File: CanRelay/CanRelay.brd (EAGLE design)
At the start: 84.6 x 65.5 mm, 20 parts

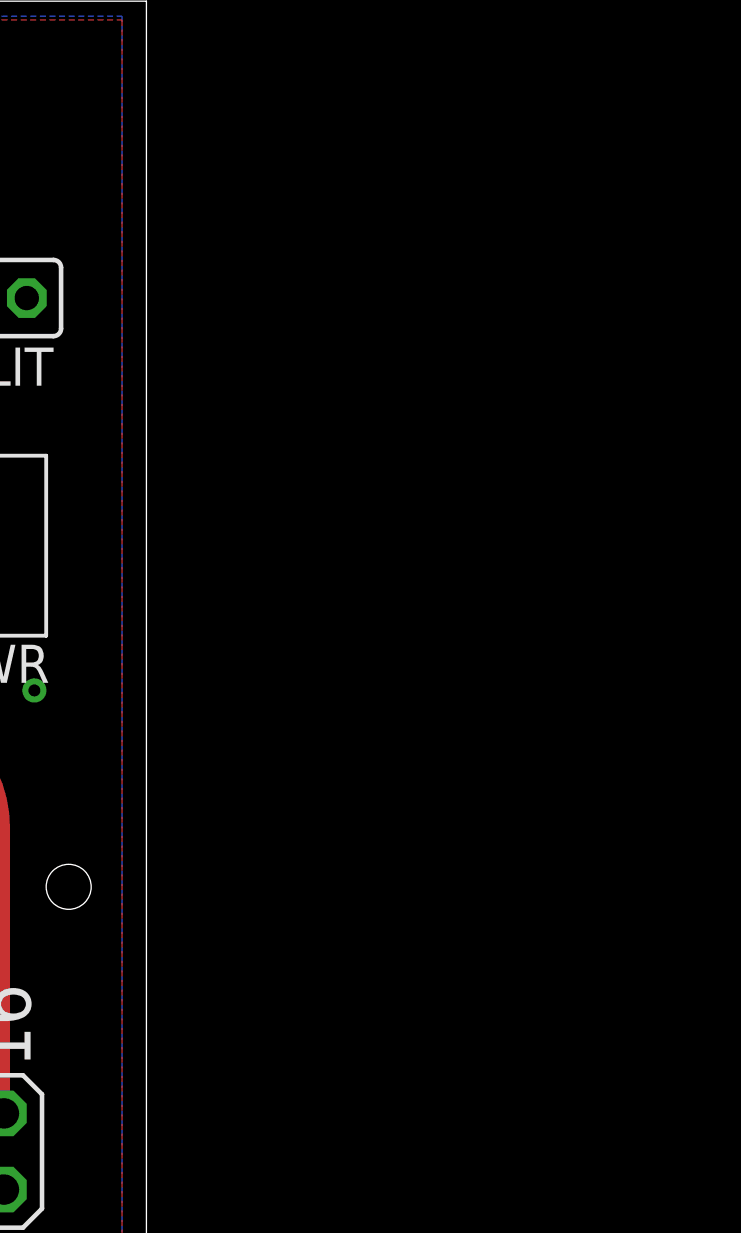
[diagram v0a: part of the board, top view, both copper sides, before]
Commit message: #12 dropping 2 new power jacks into the schematic and connecting. Only dropping into the board, not yet aligning up all
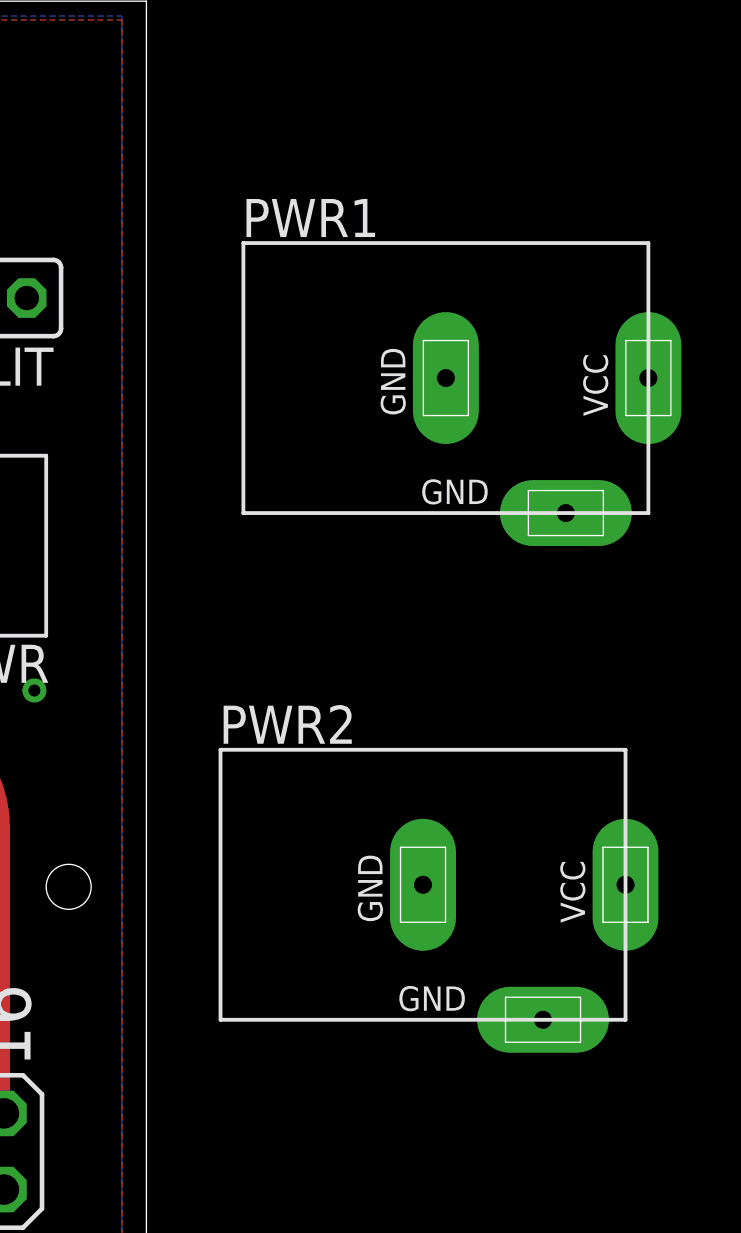
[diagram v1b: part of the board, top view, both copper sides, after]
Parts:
- added PWR1, PWR2: DC-JACK-GK2.1S, PoJD:DC-JACK-GK2.1
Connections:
- net +5V: now also PWR1.VCC, PWR2.VCC
- net GND: now also PWR1.GND1, PWR1.GND2, PWR2.GND1, PWR2.GND2
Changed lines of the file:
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@@
 <?xml version="1.0" encoding="utf-8"?>
 <!DOCTYPE eagle SYSTEM "eagle.dtd">
-<eagle version="7.6.0">
+<eagle version="7.7.0">
 <drawing>
 <settings>
@@
 <element name="XTAL" library="special" package="QS" value="16MHz" x="35.433" y="14.986" rot="R180"/>
 <element name="USBTIN" library="pinhead" package="1X03" value="" x="24.13" y="58.801" rot="R270"/>
+<element name="PWR1" library="PoJD" package="DC-JACK-GK2.1" value="DC-JACK-GK2.1S" x="94.615" y="52.959"/>
+<element name="PWR2" library="PoJD" package="DC-JACK-GK2.1" value="DC-JACK-GK2.1S" x="93.853" y="36.068"/>
 </elements>
 <signals>
@@
 <wire x1="10.033" y1="45.339" x2="8.763" y2="44.069" width="0.4064" layer="1" curve="90"/>
 <wire x1="8.763" y1="44.069" x2="8.763" y2="42.672" width="0.4064" layer="1"/>
+<contactref element="PWR1" pad="VCC"/>
+<contactref element="PWR2" pad="VCC"/>
+<wire x1="101.365" y1="52.959" x2="5.461" y2="32.385" width="0" layer="19" extent="1-1"/>
+<wire x1="100.603" y1="36.068" x2="101.365" y2="52.959" width="0" layer="19" extent="1-1"/>
 </signal>
 <signal name="GND">
@@
 <via x="55.499" y="44.577" extent="1-16" drill="0.4" shape="square"/>
 <via x="40.767" y="17.907" extent="1-16" drill="0.4" shape="square"/>
+<contactref element="PWR2" pad="GND1"/>
+<contactref element="PWR1" pad="GND1"/>
+<contactref element="PWR1" pad="GND2"/>
+<contactref element="PWR2" pad="GND2"/>
+<wire x1="80.645" y1="55.626" x2="76.073" y2="61.595" width="0" layer="19" extent="1-1"/>
+<wire x1="72.292" y1="50.371" x2="80.645" y2="55.626" width="0" layer="19" extent="1-1"/>
+<wire x1="71.492" y1="44.371" x2="72.292" y2="50.371" width="0" layer="19" extent="1-1"/>
+<wire x1="62.103" y1="44.323" x2="71.492" y2="44.371" width="0" layer="19" extent="1-1"/>
+<wire x1="62.103" y1="50.419" x2="62.103" y2="44.323" width="0" layer="19" extent="1-1"/>
+<wire x1="55.753" y1="50.292" x2="62.103" y2="50.419" width="0" layer="19" extent="1-1"/>
+<wire x1="55.499" y1="44.577" x2="55.753" y2="50.292" width="0" layer="19" extent="1-1"/>
+<wire x1="60.96" y1="36.703" x2="62.103" y2="44.323" width="0" layer="19" extent="1-1"/>
+<wire x1="47.371" y1="44.704" x2="55.499" y2="44.577" width="0" layer="19" extent="1-1"/>
+<wire x1="39.497" y1="44.577" x2="47.371" y2="44.704" width="0" layer="19" extent="1-1"/>
+<wire x1="45.339" y1="36.83" x2="47.371" y2="44.704" width="0" layer="19" extent="1-1"/>
+<wire x1="39.243" y1="35.941" x2="45.339" y2="36.83" width="0" layer="19" extent="1-1"/>
+<wire x1="36.703" y1="31.242" x2="39.243" y2="35.941" width="0" layer="19" extent="1-1"/>
+<wire x1="30.353" y1="44.704" x2="39.497" y2="44.577" width="0" layer="19" extent="1-1"/>
+<wire x1="21.463" y1="44.45" x2="30.353" y2="44.704" width="0" layer="19" extent="1-1"/>
+<wire x1="20.193" y1="50.927" x2="21.463" y2="44.45" width="0" layer="19" extent="1-1"/>
+<wire x1="24.13" y1="56.261" x2="20.193" y2="50.927" width="0" layer="19" extent="1-1"/>
+<wire x1="13.808" y1="52.822" x2="20.193" y2="50.927" width="0" layer="19" extent="1-1"/>
+<wire x1="13.808" y1="56.902" x2="13.808" y2="52.822" width="0" layer="19" extent="1-1"/>
+<wire x1="31.623" y1="23.622" x2="36.703" y2="31.242" width="0" layer="19" extent="1-1"/>
+<wire x1="29.718" y1="19.558" x2="31.623" y2="23.622" width="0" layer="19" extent="1-1"/>
+<wire x1="25.273" y1="13.716" x2="29.718" y2="19.558" width="0" layer="19" extent="1-1"/>
+<wire x1="26.924" y1="8.509" x2="25.273" y2="13.716" width="0" layer="19" extent="1-1"/>
+<wire x1="32.893" y1="7.239" x2="26.924" y2="8.509" width="0" layer="19" extent="1-1"/>
+<wire x1="37.973" y1="7.239" x2="32.893" y2="7.239" width="0" layer="19" extent="1-1"/>
+<wire x1="44.196" y1="12.827" x2="37.973" y2="7.239" width="0" layer="19" extent="1-1"/>
+<wire x1="40.767" y1="17.907" x2="44.196" y2="12.827" width="0" layer="19" extent="1-1"/>
+<wire x1="50.165" y1="8.509" x2="44.196" y2="12.827" width="0" layer="19" extent="1-1"/>
+<wire x1="49.784" y1="17.78" x2="44.196" y2="12.827" width="0" layer="19" extent="1-1"/>
+<wire x1="51.562" y1="24.765" x2="49.784" y2="17.78" width="0" layer="19" extent="1-1"/>
+<wire x1="51.562" y1="29.591" x2="51.562" y2="24.765" width="0" layer="19" extent="1-1"/>
+<wire x1="56.134" y1="13.589" x2="49.784" y2="17.78" width="0" layer="19" extent="1-1"/>
+<wire x1="60.96" y1="8.89" x2="56.134" y2="13.589" width="0" layer="19" extent="1-1"/>
+<wire x1="64.135" y1="14.224" x2="60.96" y2="8.89" width="0" layer="19" extent="1-1"/>
+<wire x1="66.167" y1="19.685" x2="64.135" y2="14.224" width="0" layer="19" extent="1-1"/>
+<wire x1="33.655" y1="56.388" x2="24.13" y2="56.261" width="0" layer="19" extent="1-1"/>
+<wire x1="38.1" y1="56.261" x2="33.655" y2="56.388" width="0" layer="19" extent="1-1"/>
+<wire x1="38.1" y1="62.992" x2="38.1" y2="56.261" width="0" layer="19" extent="1-1"/>
+<wire x1="80.899" y1="42.545" x2="71.492" y2="44.371" width="0" layer="19" extent="1-1"/>
+<wire x1="47.943" y1="58.801" x2="38.1" y2="56.261" width="0" layer="19" extent="1-1"/>
+<wire x1="55.943" y1="61.341" x2="47.943" y2="58.801" width="0" layer="19" extent="1-1"/>
+<wire x1="11.303" y1="42.672" x2="21.463" y2="44.45" width="0" layer="19" extent="1-1"/>
+<wire x1="3.556" y1="45.72" x2="11.303" y2="42.672" width="0" layer="19" extent="1-1"/>
+<wire x1="80.518" y1="16.383" x2="66.167" y2="19.685" width="0" layer="19" extent="1-1"/>
+<wire x1="80.645" y1="7.493" x2="80.518" y2="16.383" width="0" layer="19" extent="1-1"/>
+<wire x1="8.636" y1="28.067" x2="11.303" y2="42.672" width="0" layer="19" extent="1-1"/>
+<wire x1="8.128" y1="10.16" x2="25.273" y2="13.716" width="0" layer="19" extent="1-1"/>
+<wire x1="8.255" y1="3.429" x2="8.128" y2="10.16" width="0" layer="19" extent="1-1"/>
+<wire x1="4.064" y1="3.683" x2="8.255" y2="3.429" width="0" layer="19" extent="1-1"/>
+<wire x1="94.615" y1="52.959" x2="8.255" y2="3.429" width="0" layer="19" extent="1-1"/>
+<wire x1="98.615" y1="48.459" x2="94.615" y2="52.959" width="0" layer="19" extent="1-1"/>
+<wire x1="93.853" y1="36.068" x2="98.615" y2="48.459" width="0" layer="19" extent="1-1"/>
+<wire x1="97.853" y1="31.568" x2="93.853" y2="36.068" width="0" layer="19" extent="1-1"/>
 </signal>
 <signal name="N$2">

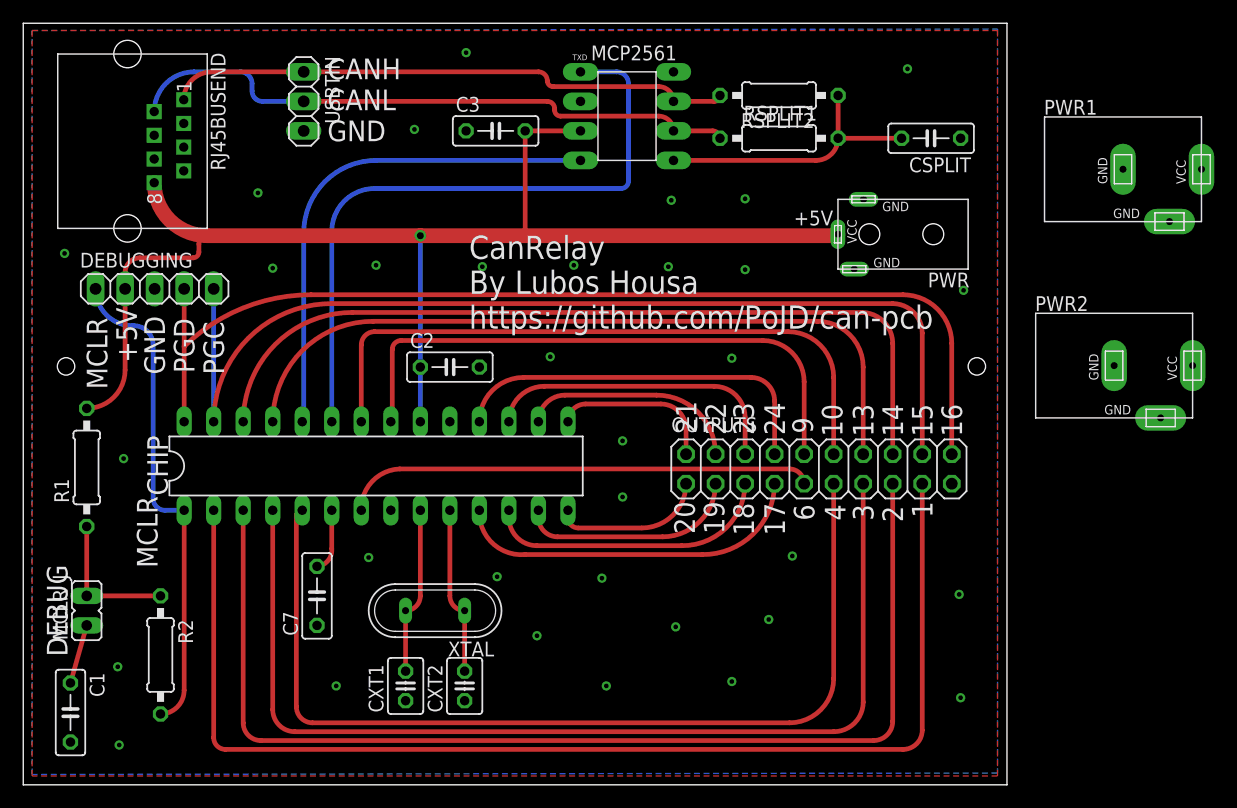
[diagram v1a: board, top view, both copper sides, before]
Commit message: #12 dropping the 2 and replacing with jut 1 new power jack, aliging all in board, not yet wiring all up since will need one more change to mirror the RJ45 connector anyway. but space now sufficient for new power jack
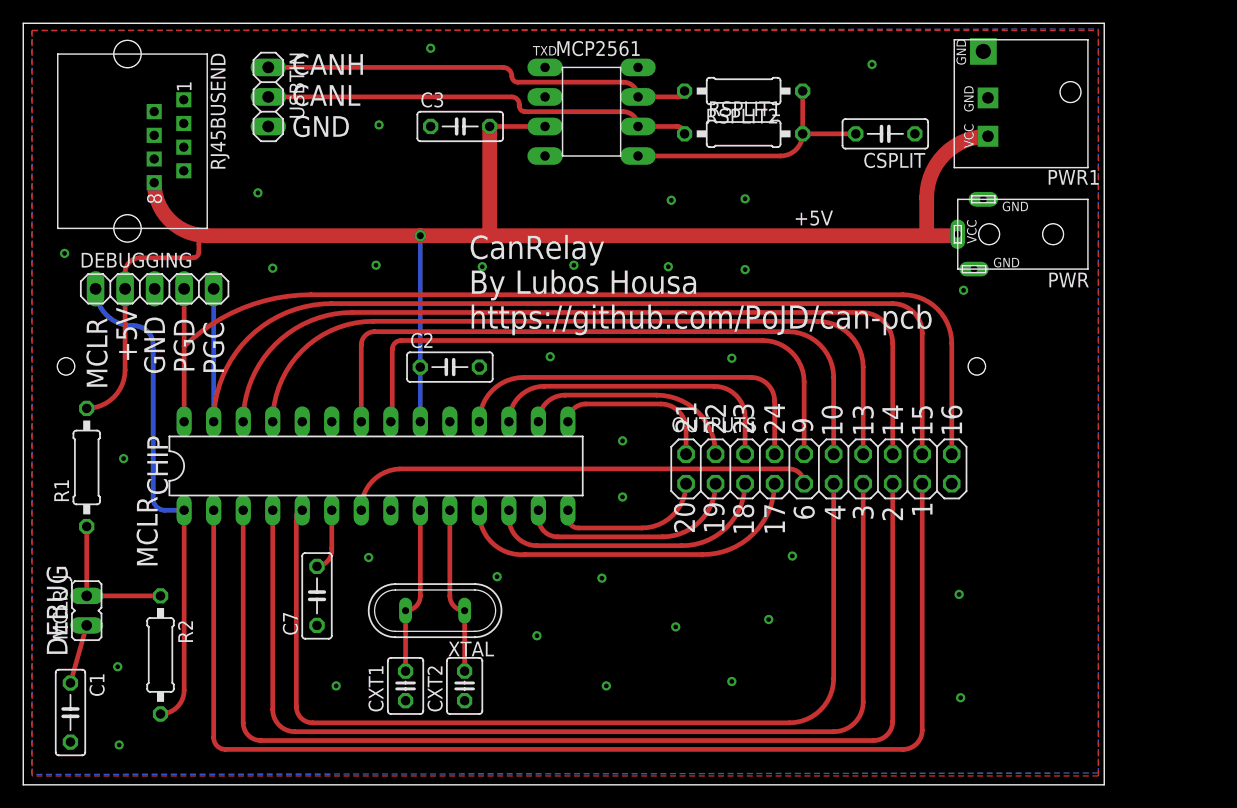
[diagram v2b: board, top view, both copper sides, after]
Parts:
- removed PWR2: DC-JACK-GK2.1S, PoJD:DC-JACK-GK2.1
- PWR1: value DC-JACK-GK2.1S -> DC-JACK-SCD-06A-2.5S; device PoJD:DC-JACK-GK2.1 -> PoJD:DC-JACK-SCD-016A-2.5
- moved PWR1 10.4 mm to (85.8, 58.6), turned to 180 degrees
- moved PWR 10.3 mm to (86.0, 47.4)
- moved CSPLIT 3.96 mm to (74.2, 56.0)
- moved C3 3.07 mm to (37.6, 56.6)
- moved RSPLIT1 3.07 mm to (62.0, 56.0)
- moved RSPLIT2 3.07 mm to (62.0, 59.7)
- moved USBTIN 3.07 mm to (21.1, 59.2)
- moved MCP2561 3.07 mm to (48.9, 57.9)
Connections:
- net +5V: no longer PWR2.VCC
- net GND: no longer PWR2.GND1, PWR2.GND2
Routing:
- net TXD: track 56.8 -> 0.18 mm
- net RXD: track 42.7 -> 0.00 mm
- net +5V: track 113.3 -> 134.8 mm
- net CANL: track 52.9 -> 37.2 mm
- net CANH: track 48.4 -> 37.1 mm
- net SPLIT: track 24.3 -> 23.5 mm
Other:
- board size 84.6 x 65.5 mm -> 93 x 65.5 mm
